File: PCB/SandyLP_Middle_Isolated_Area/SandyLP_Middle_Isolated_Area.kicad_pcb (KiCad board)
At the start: 2 copper layers, 42.3 x 20.8 mm, 18 parts

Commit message: オプションが無料になったのでJLCのマーキングを削除。その他シルク位置調整。
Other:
- board text removed: "JLCJLCJLCJLC"
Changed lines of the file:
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@@
 	(generator_version "8.0")
 	(general
-		(thickness 1.2)
+		(thickness 1.6)
 		(legacy_teardrops no)
 	)
@@
 			(layer "dielectric 1"
 				(type "core")
-				(thickness 1.11)
+				(thickness 1.51)
 				(material "FR4")
 				(epsilon_r 4.5)
@@
 		(fp_arc
 			(start 2.475824 -5.107131)
-			(mid 1.399999 -5.299999)
+			(mid 1.4 -5.3)
 			(end 0.555319 -5.993622)
 			(stroke
@@
 		(fp_arc
 			(start 0.671822 -3.333526)
-			(mid 0.262252 -3.449499)
+			(mid 0.262246 -3.449501)
 			(end 0.25 -3.875)
 			(stroke
@@
 			)
 			(justify mirror)
-		)
-	)
-	(gr_text "JLCJLCJLCJLC"
-		(at 51.083435 57.31903 0)
-		(layer "B.SilkS")
-		(effects
-			(font
-				(size 1 1)
-				(thickness 0.15)
-			)
-			(justify mirror)

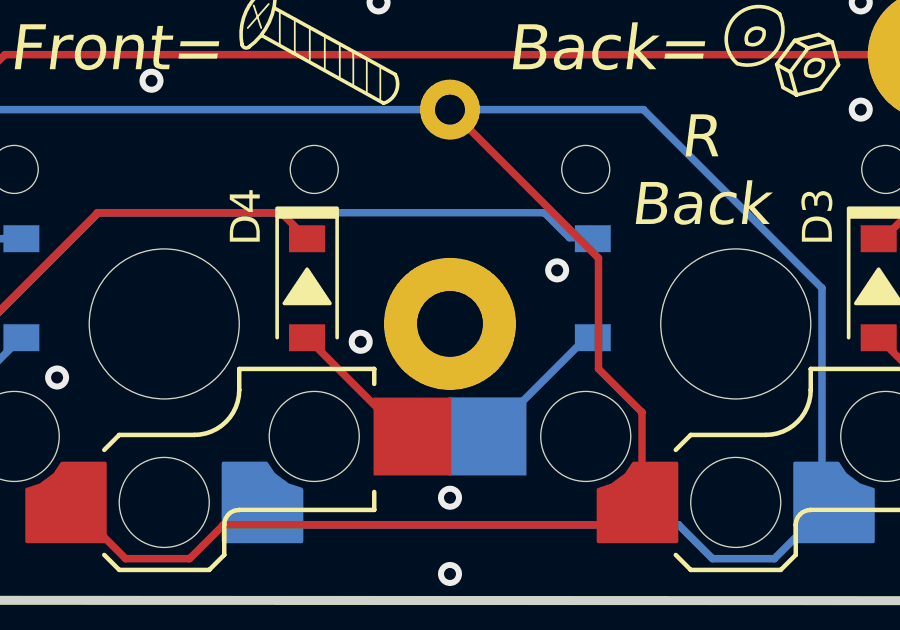
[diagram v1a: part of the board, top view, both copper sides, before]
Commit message: Mid-ISOの中央ネジがソケットのパッドに近すぎるので、少し上へ移動
USBのD+、D-なども合わせて調整。
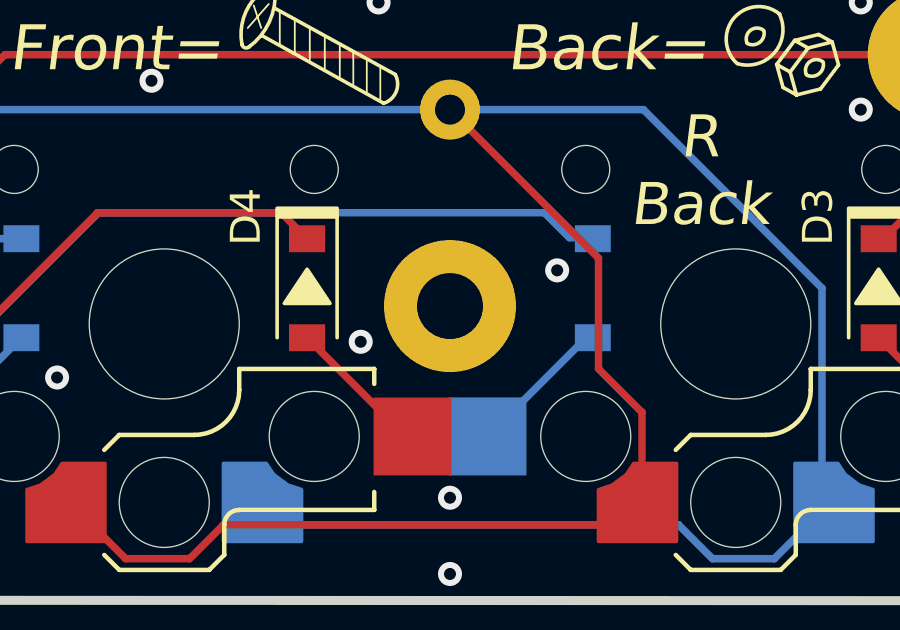
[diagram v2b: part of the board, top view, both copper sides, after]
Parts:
- moved H4 0.60 mm to (49.6, 49.0)
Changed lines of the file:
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@@
 		(fp_arc
 			(start 2.475824 -5.107131)
-			(mid 1.4 -5.3)
+			(mid 1.399999 -5.299999)
 			(end 0.555319 -5.993622)
 			(stroke
@@
 		(fp_arc
 			(start 0.671822 -3.333526)
-			(mid 0.262246 -3.449501)
+			(mid 0.262252 -3.449499)
 			(end 0.25 -3.875)
 			(stroke
@@
 	(footprint "locallib:MountingHole_2.2mm_M2_Pad_minimal"
 		(layer "B.Cu")
-		(at 49.633435 49.62528 180)
+		(at 49.633435 49.029977 180)
 		(descr "Mounting Hole 2.2mm, M2")
 		(tags "mounting hole 2.2mm m2")

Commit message: ネジとソケットのパッドか近くはんだ付けが心配なため、パッドを少し小さくする。
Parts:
- SW_TAB1: footprint locallib:Kailh_socket_ChocV2_for_Reverse -> locallib:Kailh_socket_ChocV2_for_Reverse_narrow_#2pad
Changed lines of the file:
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@@
 		(fp_arc
 			(start 2.475824 -5.107131)
-			(mid 1.399999 -5.299999)
+			(mid 1.4 -5.3)
 			(end 0.555319 -5.993622)
 			(stroke
@@
 		)
 	)
-	(footprint "locallib:Kailh_socket_ChocV2_for_Reverse"
+	(footprint "locallib:Kailh_socket_ChocV2_for_Reverse_narrow_#2pad"
 		(layer "F.Cu")
 		(at 40.108435 49.62528)
@@
 			)
 		)
-		(property "Footprint" "locallib:Kailh_socket_ChocV2_for_Reverse"
+		(property "Footprint" "locallib:Kailh_socket_ChocV2_for_Reverse_narrow_#2pad"
 			(at 0 0 0)
 			(layer "F.Fab")
@@
 		)
 		(pad "2" smd rect
-			(at -8.275 3.75)
-			(size 2.6 2.6)
+			(at -8.275 3.65)
+			(size 2.6 2.4)
 			(layers "B.Cu" "B.Paste" "B.Mask")
 			(net 1 "Net-(D1-A)")
@@
 		(fp_arc
 			(start 0.671822 -3.333526)
-			(mid 0.262252 -3.449499)
+			(mid 0.262246 -3.449501)
 			(end 0.25 -3.875)
 			(stroke

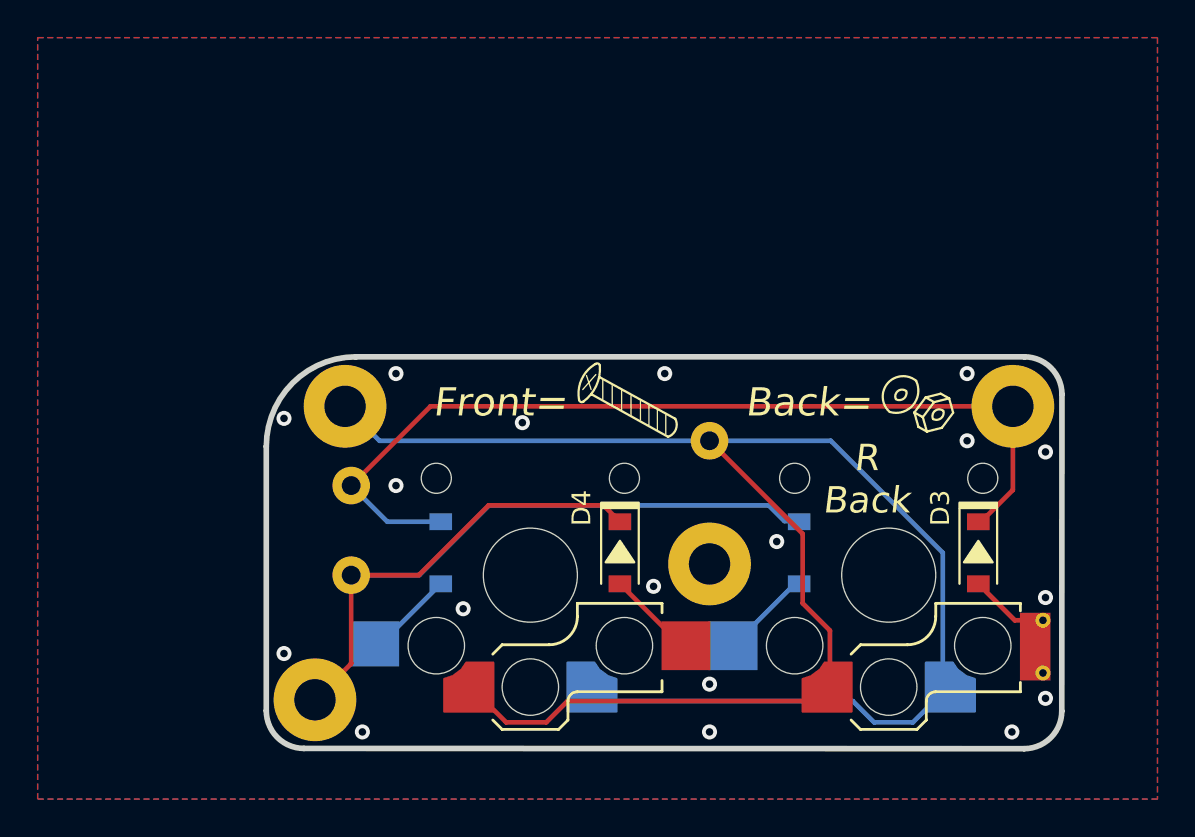
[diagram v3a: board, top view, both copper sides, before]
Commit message: Mid-ISO基板　ゴムシート貼り付け指標
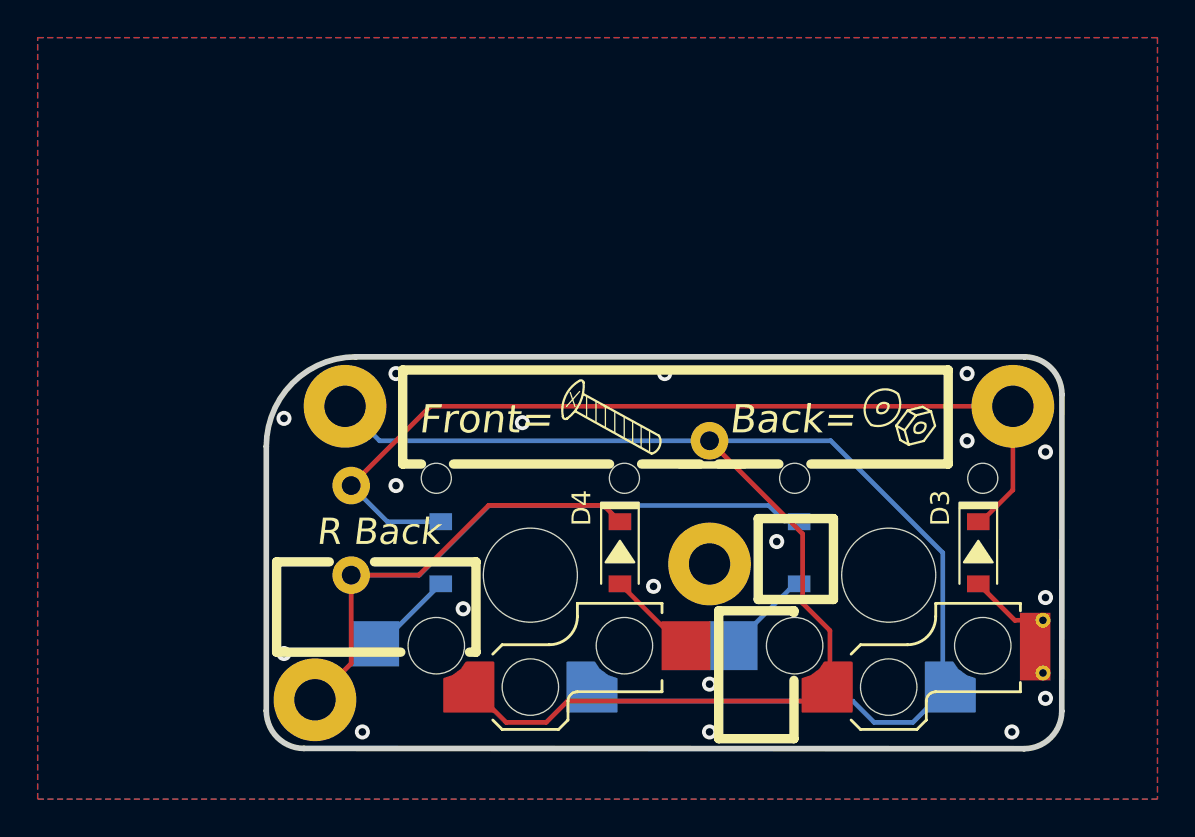
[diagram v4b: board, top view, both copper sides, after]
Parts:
- moved REF** 1.25 mm to (48.0, 41.9)
- moved REF** 1.19 mm to (57.2, 41.3)
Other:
- board text added: "#SandyLP_kbd DN0010"
- board text added: "Mid-Iso by @jpskenn"
- board text removed: "#SandyLP_kbd DN0010 Mid-Iso by @jpskenn"
